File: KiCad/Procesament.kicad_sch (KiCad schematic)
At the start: 4 parts, among them U4 Pic24hj128gp502

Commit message: Programador
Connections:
- net GND: now also U4.24 (AVss)
- net VCC: now also U4.25 (AVdd)
- net PGD: now reaches U4.1 (RB0)
- net PGC: now reaches U4.2 (RB1)
- net MCLR: now reaches U4.26 (~{MCLR}/VPP/RE3)
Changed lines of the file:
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@@
+	(wire
+		(pts
+			(xy 137.16 76.2) (xy 149.86 76.2)
+		)
+		(stroke
+			(width 0)
+			(type default)
+		)
+	)
 	(wire
 		(pts
@@
 		)
 	)
+	(global_label "PGD"
+		(shape input)
+		(at 101.6 40.64 180)
+		(fields_autoplaced yes)
+		(effects
+			(font
+				(size 1.27 1.27)
+			)
+			(justify right)
+		)
+		(property "Intersheetrefs" "${INTERSHEET_REFS}"
+			(at 94.8048 40.64 0)
+			(effects
+				(font
+					(size 1.27 1.27)
+				)
+				(justify right)
+				(hide yes)
+			)
+		)
+	)
+	(global_label "PGC"
+		(shape input)
+		(at 101.6 43.18 180)
+		(fields_autoplaced yes)
+		(effects
+			(font
+				(size 1.27 1.27)
+			)
+			(justify right)
+		)
+		(property "Intersheetrefs" "${INTERSHEET_REFS}"
+			(at 94.8048 43.18 0)
+			(effects
+				(font
+					(size 1.27 1.27)
+				)
+				(justify right)
+				(hide yes)
+			)
+		)
+	)
 	(global_label "OSC1"
 		(shape output)
@@
 		)
 	)
+	(global_label "MCLR"
+		(shape input)
+		(at 137.16 78.74 0)
+		(fields_autoplaced yes)
+		(effects
+			(font
+				(size 1.27 1.27)
+			)
+			(justify left)
+		)
+		(property "Intersheetrefs" "${INTERSHEET_REFS}"
+			(at 145.1647 78.74 0)
+			(effects
+				(font
+					(size 1.27 1.27)
+				)
+				(justify left)
+				(hide yes)
+			)
+		)
+	)
 	(global_label "VCC"
 		(shape input)
@@
 		)
 	)
+	(global_label "VCC"
+		(shape input)
+		(at 137.16 73.66 0)
+		(fields_autoplaced yes)
+		(effects
+			(font
+				(size 1.27 1.27)
+			)
+			(justify left)
+		)
+		(property "Intersheetrefs" "${INTERSHEET_REFS}"
+			(at 143.7738 73.66 0)
+			(effects
+				(font
+					(size 1.27 1.27)
+				)
+				(justify left)
+				(hide yes)
+			)
+		)
+	)
 	(global_label "OSC1"
 		(shape input)
@@
 			)
 		)
+	)
+	(symbol
+		(lib_id "power:GND")
+		(at 149.86 76.2 0)
+		(unit 1)
+		(exclude_from_sim no)
+		(in_bom yes)
+		(on_board yes)
+		(dnp no)
+		(fields_autoplaced yes)
+		(property "Reference" "#PWR039"
+			(at 149.86 82.55 0)
+			(effects
+				(font
+					(size 1.27 1.27)
+				)
+				(hide yes)
+			)
+		)
+		(property "Value" "GND"
+			(at 149.86 81.28 0)
+			(effects
+				(font
+					(size 1.27 1.27)
+				)
+			)
+		)
+		(property "Footprint" ""
+			(at 149.86 76.2 0)
+			(effects
+				(font
+					(size 1.27 1.27)
+				)
+				(hide yes)
+			)
+		)
+		(property "Datasheet" ""
+			(at 149.86 76.2 0)
+			(effects
+				(font
+					(size 1.27 1.27)
+				)
+				(hide yes)
+			)
+		)
+		(property "Description" "Power symbol creates a global label with name \"GND\" , ground"
+			(at 149.86 76.2 0)
+			(effects
+				(font
+					(size 1.27 1.27)
+				)
+				(hide yes)
+			)
+		)
+		(pin "1"
+		)
+		(instances
+			(project "Grup_D_Llums"
+				(path "/88ef36bc-9439-47f2-adb5-e1da6bb8c9dd/d0e5a634-ab84-467f-83ee-5a846a1f3782"
+					(reference "#PWR039")
+					(unit 1)
+				)
+			)
+		)

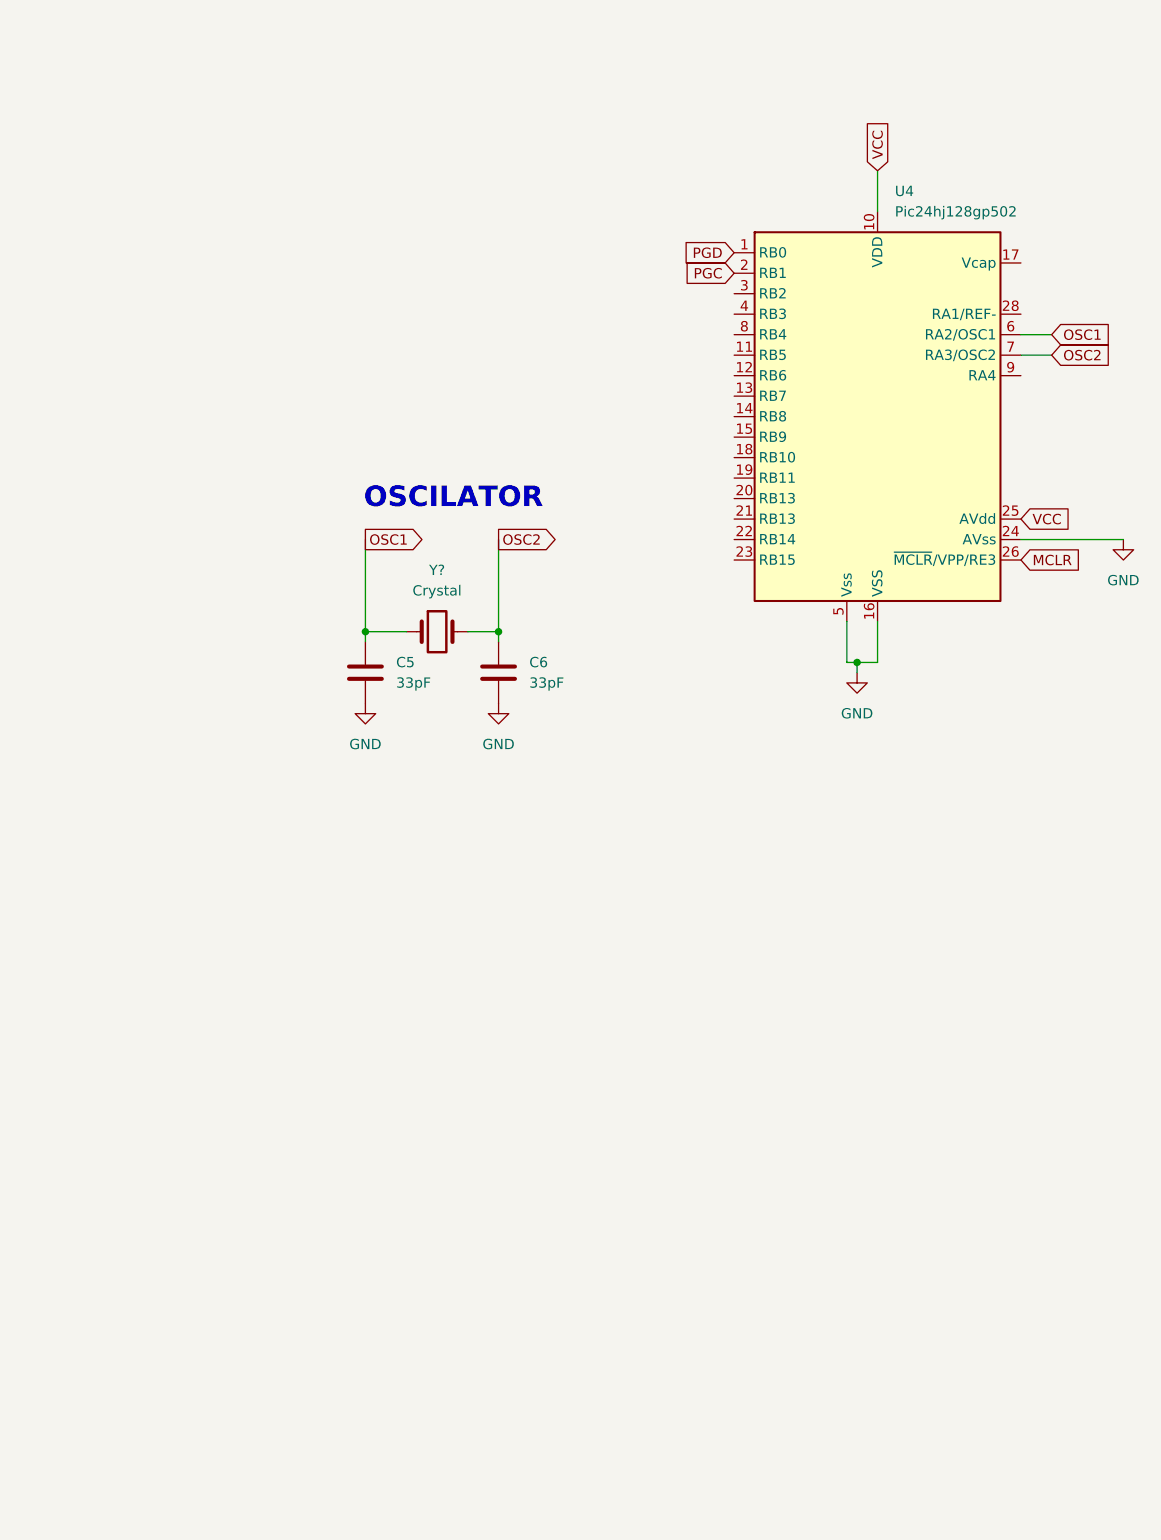
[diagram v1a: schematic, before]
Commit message: acabar can, estil y micro biel
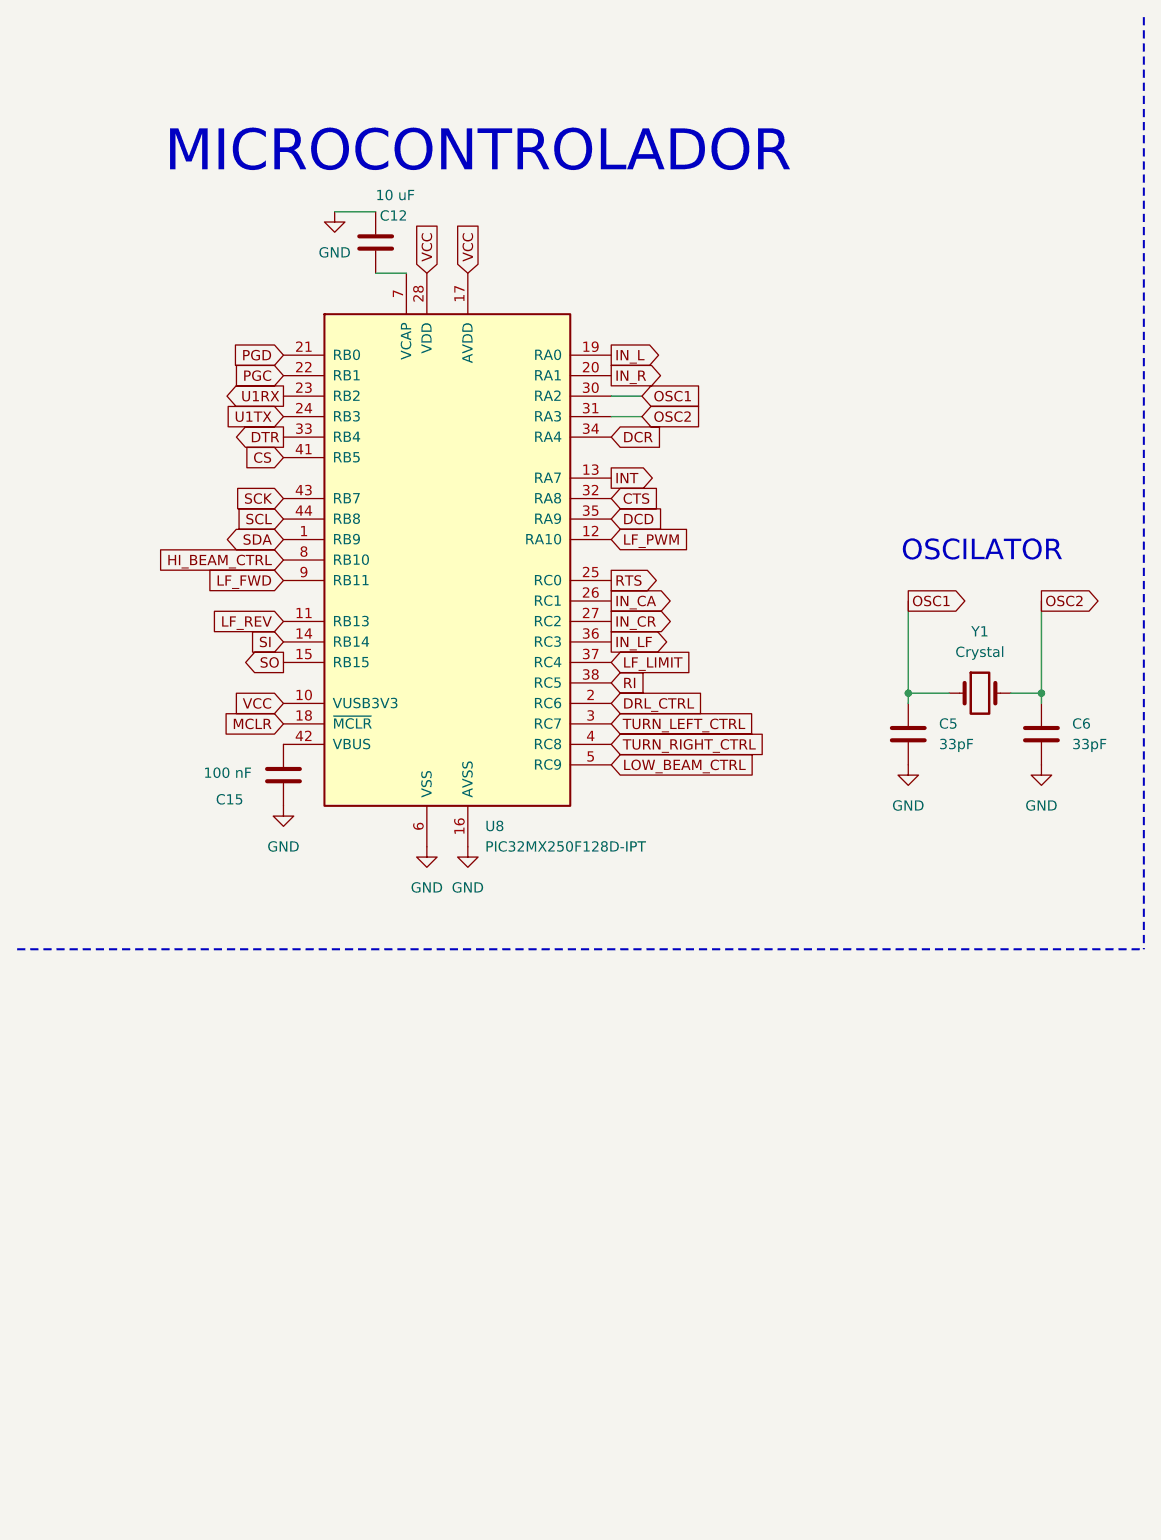
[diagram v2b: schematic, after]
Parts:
- removed U4: Pic24hj128gp502, Package_SO:SOIC-28W_7.5x17.9mm_P1.27mm, symbol simbolo:Pic24hj128gp502
- added C12: 10 uF, symbol Device:C
- added C15: 100 nF, symbol Device:C
- added U8: PIC32MX250F128D-IPT, Package_QFP:TQFP-44_10x10mm_P0.8mm, symbol MCU_Microchip_PIC32:PIC32MX250F128D-IPT
- gave numbers to parts that had none: 1
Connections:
- net GND: now also C12.1, C15.2, U8.16 (AVSS), U8.29 (VSS), U8.39 (VSS), U8.6 (VSS)
- net MCLR: now also U8.18 (~{MCLR})
- net OSC1: now also U8.30 (RA2)
- net OSC2: now also U8.31 (RA3)
- net PGC: now also U8.22 (RB1)
- net PGD: now also U8.21 (RB0)
- net VCC: now also U8.10 (VUSB3V3), U8.17 (AVDD), U8.28 (VDD), U8.40 (VDD)
- new net: C15.1, U8.42 (VBUS)
- new net: C12.2, U8.7 (VCAP)
- new net CS: U8.41 (RB5)
- new net CTS: U8.32 (RA8)
- new net DCD: U8.35 (RA9)
- new net DCR: U8.34 (RA4)
- new net DRL_CTRL: U8.2 (RC6)
- new net DTR: U8.33 (RB4)
- new net HI_BEAM_CTRL: U8.8 (RB10)
- new net INT: U8.13 (RA7)
- new net IN_CA: U8.26 (RC1)
- new net IN_CR: U8.27 (RC2)
- new net IN_L: U8.19 (RA0)
- new net IN_LF: U8.36 (RC3)
- new net IN_R: U8.20 (RA1)
- new net LF_FWD: U8.9 (RB11)
- new net LF_LIMIT: U8.37 (RC4)
- new net LF_PWM: U8.12 (RA10)
- new net LF_REV: U8.11 (RB13)
- new net LOW_BEAM_CTRL: U8.5 (RC9)
- new net RI: U8.38 (RC5)
- new net RTS: U8.25 (RC0)
- new net SCK: U8.43 (RB7)
- new net SCL: U8.44 (RB8)
- new net SDA: U8.1 (RB9)
- new net SI: U8.14 (RB14)
- new net SO: U8.15 (RB15)
- new net TURN_LEFT_CTRL: U8.3 (RC7)
- new net TURN_RIGHT_CTRL: U8.4 (RC8)
- new net U1RX: U8.23 (RB2)
- new net U1TX: U8.24 (RB3)
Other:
- note added: "MICROCONTROLADOR"
- moved on the sheet: C5, C6, Y1

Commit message: Debugging
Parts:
- added J2: Conn_PIC_ICSP_ICD, symbol Connector:Conn_PIC_ICSP_ICD
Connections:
- net GND: now also J2.3 (VSS)
- net MCLR: now also J2.1 (~{MCLR}/VPP)
- net PGC: now also J2.5 (PGC/ICSPCLK)
- net PGD: now also J2.4 (PGD/ICSPDAT)
- net VCC: now also J2.2 (VDD)
- no-connect marks 0 -> 1
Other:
- note added: "PROGRAMACIÓ"

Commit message: frecuencia del reloj
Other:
- note added: "8 MHZ"
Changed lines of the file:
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@@
+		)
+	)
+	(text "8 MHZ"
+		(exclude_from_sim no)
+		(at 132.334 90.932 0)
+		(effects
+			(font
+				(size 1.27 1.27)
+				(thickness 0.254)
+				(bold yes)
+			)
 		)
 	)
@@
 	(global_label "OSC1"
 		(shape output)
-		(at 123.19 83.82 0)
-		(fields_autoplaced yes)
-		(effects
-			(font
-				(size 1.27 1.27)
-			)
-			(justify left)
-		)
-		(property "Intersheetrefs" "${INTERSHEET_REFS}"
-			(at 131.1947 83.82 0)
-			(effects
-				(font
-					(size 1.27 1.27)
-				)
-				(justify left)
+		(at 123.19 83.82 180)
+		(fields_autoplaced yes)
+		(effects
+			(font
+				(size 1.27 1.27)
+			)
+			(justify right)
+		)
+		(property "Intersheetrefs" "${INTERSHEET_REFS}"
+			(at 115.1853 83.82 0)
+			(effects
+				(font
+					(size 1.27 1.27)
+				)
+				(justify right)
 				(hide yes)
 			)
@@
 		(on_board yes)
 		(dnp no)
-		(fields_autoplaced yes)
 		(property "Reference" "Y1"
-			(at 132.08 87.63 0)
+			(at 132.334 84.836 0)
 			(effects
 				(font
@@
 		)
 		(property "Value" "Crystal"
-			(at 132.08 90.17 0)
-			(effects
-				(font
+			(at 132.334 87.376 0)
+			(effects
+				(font

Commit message: titulos
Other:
- title: (none) -> Procesament
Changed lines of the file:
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@@
 	(paper "A4")
 	(title_block
+		(title "Procesament")
 		(date "2026-03-16")
 	)
